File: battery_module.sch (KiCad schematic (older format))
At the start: 15 parts

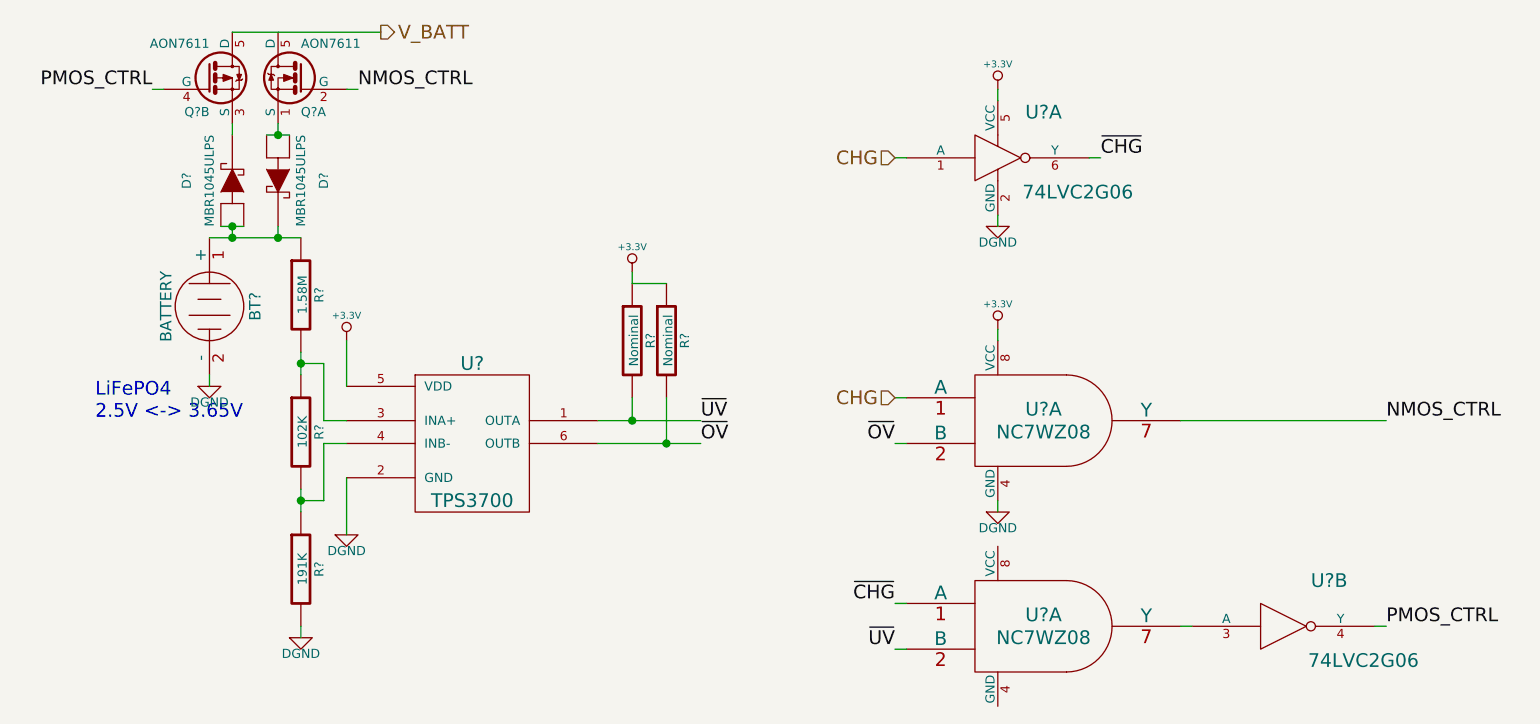
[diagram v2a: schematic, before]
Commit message: various fixes due to issues found in ERC
learned how to use invisible pins
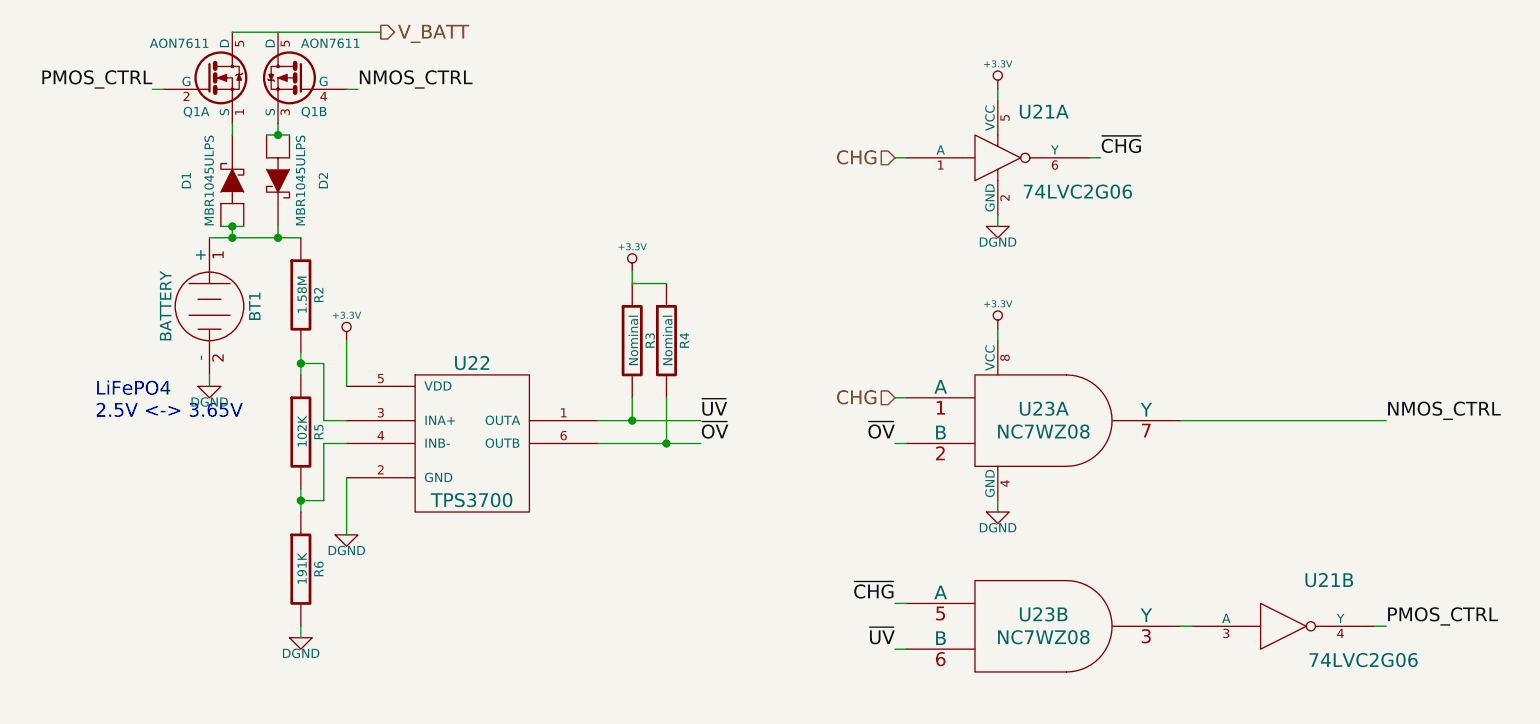
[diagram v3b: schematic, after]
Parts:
- gave numbers to parts that had none: 12
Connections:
- net NMOS_CTRL: now also Q2.4 (G); no longer Q2.2 (G)
- net PMOS_CTRL: now also Q2.2 (G); no longer Q2.4 (G)
- net ~CHG: now also U26.5 (A); no longer U26.1 (A)
- net ~UV: now also U26.6 (B); no longer U26.2 (B)
- net at U24.3 (A): now also U26.3 (Y); no longer U26.7 (Y)
- net at D4.1 (Anode), D4.2 (Anode): now also Q2.3 (S); no longer Q2.1 (S)
- net at D3.3 (Cathode): now also Q2.1 (S); no longer Q2.3 (S)

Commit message: gave parts unique id's
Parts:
- renumbered BT2 to BT1, D3 to D1, D4 to D2, Q2 to Q1, R7 to R2, R8 to R3, R9 to R4, R10 to R5, R11 to R6, U24 to U21, U25 to U22, U26 to U23
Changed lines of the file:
@@
 $Descr A4 11693 8268
 encoding utf-8
-Sheet 4 18
+Sheet 3 18
 Title ""
-Date "21 dec 2013"
+Date "12 jan 2014"
 Rev ""
 Comp ""
@@
 $EndDescr
 $Comp
-L BATTERY BT2
+L BATTERY BT1
 U 1 1 5281D336
 P 1300 1800
+AR Path="/5224C457/5281D330/5281D336" Ref="BT1"  Part="1"
 AR Path="/5224C457/5281E180/5281D336" Ref="BT2"  Part="1"
-AR Path="/5224C457/5281D330/5281D336" Ref="BT1"  Part="1"
 AR Path="/5224C457/5281E2A4/5281D336" Ref="BT3"  Part="1"
 F 0 "BT1" H 1300 2000 50  0000 C CNN
@@
 $EndComp
 $Comp
-L TPS3700 U25
+L TPS3700 U22
 U 1 1 5281D33C
 P 2450 2100
+AR Path="/5224C457/5281D330/5281D33C" Ref="U22"  Part="1"
 AR Path="/5224C457/5281E180/5281D33C" Ref="U25"  Part="1"
-AR Path="/5224C457/5281D330/5281D33C" Ref="U22"  Part="1"
 AR Path="/5224C457/5281E2A4/5281D33C" Ref="U28"  Part="1"
 F 0 "U22" H 2450 2150 60  0000 C CNN
@@
 $EndComp
 $Comp
-L R R7
+L R R2
 U 1 1 5281D342
 P 1700 1750
+AR Path="/5224C457/5281D330/5281D342" Ref="R2"  Part="1"
 AR Path="/5224C457/5281E180/5281D342" Ref="R7"  Part="1"
-AR Path="/5224C457/5281D330/5281D342" Ref="R2"  Part="1"
 AR Path="/5224C457/5281E2A4/5281D342" Ref="R12"  Part="1"
 F 0 "R2" V 1780 1750 40  0000 C CNN
@@
 $EndComp
 $Comp
-L R R10
+L R R5
 U 1 1 5281D348
 P 1700 2350
+AR Path="/5224C457/5281D330/5281D348" Ref="R5"  Part="1"
 AR Path="/5224C457/5281E180/5281D348" Ref="R10"  Part="1"
-AR Path="/5224C457/5281D330/5281D348" Ref="R5"  Part="1"
 AR Path="/5224C457/5281E2A4/5281D348" Ref="R15"  Part="1"
 F 0 "R5" V 1780 2350 40  0000 C CNN
@@
 $EndComp
 $Comp
-L R R11
+L R R6
 U 1 1 5281D34E
 P 1700 2950
+AR Path="/5224C457/5281D330/5281D34E" Ref="R6"  Part="1"
 AR Path="/5224C457/5281E180/5281D34E" Ref="R11"  Part="1"
-AR Path="/5224C457/5281D330/5281D34E" Ref="R6"  Part="1"
 AR Path="/5224C457/5281E2A4/5281D34E" Ref="R16"  Part="1"
 F 0 "R6" V 1780 2950 40  0000 C CNN
@@
 $EndComp
 $Comp
-L DGND #PWR017
+L DGND #PWR08
 U 1 1 5281D354
 P 1700 3250
+AR Path="/5224C457/5281D330/5281D354" Ref="#PWR08"  Part="1"
 AR Path="/5224C457/5281E180/5281D354" Ref="#PWR017"  Part="1"
-AR Path="/5224C457/5281D330/5281D354" Ref="#PWR08"  Part="1"
 AR Path="/5224C457/5281E2A4/5281D354" Ref="#PWR026"  Part="1"
 F 0 "#PWR08" H 1700 3250 40  0001 C CNN
@@
 $EndComp
 $Comp
-L DGND #PWR018
+L DGND #PWR09
 U 1 1 5281D35A
 P 1300 2150
+AR Path="/5224C457/5281D330/5281D35A" Ref="#PWR09"  Part="1"
 AR Path="/5224C457/5281E180/5281D35A" Ref="#PWR018"  Part="1"
-AR Path="/5224C457/5281D330/5281D35A" Ref="#PWR09"  Part="1"
 AR Path="/5224C457/5281E2A4/5281D35A" Ref="#PWR027"  Part="1"
 F 0 "#PWR09" H 1300 2150 40  0001 C CNN
@@
 $EndComp
 $Comp
-L DGND #PWR019
+L DGND #PWR010
 U 1 1 5281D360
 P 1900 2800
+AR Path="/5224C457/5281D330/5281D360" Ref="#PWR010"  Part="1"
 AR Path="/5224C457/5281E180/5281D360" Ref="#PWR019"  Part="1"
-AR Path="/5224C457/5281D330/5281D360" Ref="#PWR010"  Part="1"
 AR Path="/5224C457/5281E2A4/5281D360" Ref="#PWR028"  Part="1"
 F 0 "#PWR010" H 1900 2800 40  0001 C CNN
@@
 $EndComp
 $Comp
-L +3.3V #PWR020
+L +3.3V #PWR011
 U 1 1 5281D366
 P 1900 1950
+AR Path="/5224C457/5281D330/5281D366" Ref="#PWR011"  Part="1"
 AR Path="/5224C457/5281E180/5281D366" Ref="#PWR020"  Part="1"
-AR Path="/5224C457/5281D330/5281D366" Ref="#PWR011"  Part="1"
 AR Path="/5224C457/5281E2A4/5281D366" Ref="#PWR029"  Part="1"
 F 0 "#PWR011" H 1900 1910 30  0001 C CNN
@@
 $EndComp
 $Comp
-L R R8
+L R R3
 U 1 1 5281D36C
 P 3150 1950
+AR Path="/5224C457/5281D330/5281D36C" Ref="R3"  Part="1"
 AR Path="/5224C457/5281E180/5281D36C" Ref="R8"  Part="1"
-AR Path="/5224C457/5281D330/5281D36C" Ref="R3"  Part="1"
 AR Path="/5224C457/5281E2A4/5281D36C" Ref="R13"  Part="1"
 F 0 "R3" V 3230 1950 40  0000 C CNN
@@
 $EndComp
 $Comp
-L R R9
+L R R4
 U 1 1 5281D372
 P 3300 1950
+AR Path="/5224C457/5281D330/5281D372" Ref="R4"  Part="1"
 AR Path="/5224C457/5281E180/5281D372" Ref="R9"  Part="1"
-AR Path="/5224C457/5281D330/5281D372" Ref="R4"  Part="1"
 AR Path="/5224C457/5281E2A4/5281D372" Ref="R14"  Part="1"
 F 0 "R4" V 3380 1950 40  0000 C CNN
@@
 $EndComp
 $Comp
-L +3.3V #PWR021
+L +3.3V #PWR012
 U 1 1 5281D378
 P 3150 1650
+AR Path="/5224C457/5281D330/5281D378" Ref="#PWR012"  Part="1"
 AR Path="/5224C457/5281E180/5281D378" Ref="#PWR021"  Part="1"
-AR Path="/5224C457/5281D330/5281D378" Ref="#PWR012"  Part="1"
 AR Path="/5224C457/5281E2A4/5281D378" Ref="#PWR030"  Part="1"
 F 0 "#PWR012" H 3150 1610 30  0001 C CNN
@@
 CHG
 $Comp
-L 74LVC2G06 U24
+L 74LVC2G06 U21
 U 1 1 5281D380
 P 4750 1150
+AR Path="/5224C457/5281D330/5281D380" Ref="U21"  Part="1"
 AR Path="/5224C457/5281E180/5281D380" Ref="U24"  Part="1"
-AR Path="/5224C457/5281D330/5281D380" Ref="U21"  Part="1"
 AR Path="/5224C457/5281E2A4/5281D380" Ref="U27"  Part="1"
 F 0 "U21" H 4950 1350 60  0000 C CNN
@@
 $EndComp
 $Comp
-L 74LVC2G06 U24
+L 74LVC2G06 U21
 U 2 1 5281D386
 P 6000 3200
+AR Path="/5224C457/5281D330/5281D386" Ref="U21"  Part="2"
 AR Path="/5224C457/5281E180/5281D386" Ref="U24"  Part="2"
-AR Path="/5224C457/5281D330/5281D386" Ref="U21"  Part="2"
 AR Path="/5224C457/5281E2A4/5281D386" Ref="U27"  Part="2"
 F 0 "U21" H 6200 3400 60  0000 C CNN
@@
 $EndComp
 $Comp
-L DGND #PWR022
+L DGND #PWR013
 U 1 1 5281D38C
 P 4750 1450
+AR Path="/5224C457/5281D330/5281D38C" Ref="#PWR013"  Part="1"
 AR Path="/5224C457/5281E180/5281D38C" Ref="#PWR022"  Part="1"
-AR Path="/5224C457/5281D330/5281D38C" Ref="#PWR013"  Part="1"
 AR Path="/5224C457/5281E2A4/5281D38C" Ref="#PWR031"  Part="1"
 F 0 "#PWR013" H 4750 1450 40  0001 C CNN
@@
 $EndComp
 $Comp
-L +3.3V #PWR023
+L +3.3V #PWR014
 U 1 1 5281D392
 P 4750 850
+AR Path="/5224C457/5281D330/5281D392" Ref="#PWR014"  Part="1"
 AR Path="/5224C457/5281E180/5281D392" Ref="#PWR023"  Part="1"
-AR Path="/5224C457/5281D330/5281D392" Ref="#PWR014"  Part="1"
 AR Path="/5224C457/5281E2A4/5281D392" Ref="#PWR032"  Part="1"
 F 0 "#PWR014" H 4750 810 30  0001 C CNN
@@
 $EndComp
 $Comp
-L NC7WZ08 U26
+L NC7WZ08 U23
 U 1 1 5281D398
 P 4950 2300
+AR Path="/5224C457/5281D330/5281D398" Ref="U23"  Part="1"
 AR Path="/5224C457/5281E180/5281D398" Ref="U26"  Part="1"
-AR Path="/5224C457/5281D330/5281D398" Ref="U23"  Part="1"
 AR Path="/5224C457/5281E2A4/5281D398" Ref="U29"  Part="1"
 F 0 "U23" H 4950 2350 60  0000 C CNN
@@
 $EndComp
 $Comp
-L NC7WZ08 U26
+L NC7WZ08 U23
 U 2 1 5281D39E
 P 4950 3200
+AR Path="/5224C457/5281D330/5281D39E" Ref="U23"  Part="2"
 AR Path="/5224C457/5281E180/5281D39E" Ref="U26"  Part="2"
-AR Path="/5224C457/5281D330/5281D39E" Ref="U23"  Part="2"
 AR Path="/5224C457/5281E2A4/5281D39E" Ref="U29"  Part="2"
 F 0 "U23" H 4950 3250 60  0000 C CNN
@@
 NMOS_CTRL
 $Comp
-L DGND #PWR024
+L DGND #PWR015
 U 1 1 5281D3A6
 P 4750 2700
+AR Path="/5224C457/5281D330/5281D3A6" Ref="#PWR015"  Part="1"
 AR Path="/5224C457/5281E180/5281D3A6" Ref="#PWR024"  Part="1"
-AR Path="/5224C457/5281D330/5281D3A6" Ref="#PWR015"  Part="1"
 AR Path="/5224C457/5281E2A4/5281D3A6" Ref="#PWR033"  Part="1"
 F 0 "#PWR015" H 4750 2700 40  0001 C CNN
@@
 $EndComp
 $Comp
-L +3.3V #PWR025
+L +3.3V #PWR016
 U 1 1 5281D3AC
 P 4750 1900
+AR Path="/5224C457/5281D330/5281D3AC" Ref="#PWR016"  Part="1"
 AR Path="/5224C457/5281E180/5281D3AC" Ref="#PWR025"  Part="1"
-AR Path="/5224C457/5281D330/5281D3AC" Ref="#PWR016"  Part="1"
 AR Path="/5224C457/5281E2A4/5281D3AC" Ref="#PWR034"  Part="1"
 F 0 "#PWR016" H 4750 1860 30  0001 C CNN
@@
 ~CHG
 $Comp
-L AON7611 Q2
+L AON7611 Q1
 U 2 1 5281D3B9
 P 1700 800
+AR Path="/5224C457/5281D330/5281D3B9" Ref="Q1"  Part="2"
 AR Path="/5224C457/5281E180/5281D3B9" Ref="Q2"  Part="2"
-AR Path="/5224C457/5281D330/5281D3B9" Ref="Q1"  Part="2"
 AR Path="/5224C457/5281E2A4/5281D3B9" Ref="Q3"  Part="2"
 F 0 "Q1" H 1700 651 40  0000 R CNN
@@
 $EndComp
 $Comp
-L AON7611 Q2
+L AON7611 Q1
 U 1 1 5281D3BF
 P 1300 800
+AR Path="/5224C457/5281D330/5281D3BF" Ref="Q1"  Part="1"
 AR Path="/5224C457/5281E180/5281D3BF" Ref="Q2"  Part="1"
-AR Path="/5224C457/5281D330/5281D3BF" Ref="Q1"  Part="1"
 AR Path="/5224C457/5281E2A4/5281D3BF" Ref="Q3"  Part="1"
 F 0 "Q1" H 1300 651 40  0000 R CNN
@@
 PMOS_CTRL
 $Comp
-L MBR1045ULPS D3
+L MBR1045ULPS D1
 U 1 1 5281D3C7
 P 1400 1250
+AR Path="/5224C457/5281D330/5281D3C7" Ref="D1"  Part="1"
 AR Path="/5224C457/5281E180/5281D3C7" Ref="D3"  Part="1"
-AR Path="/5224C457/5281D330/5281D3C7" Ref="D1"  Part="1"
 AR Path="/5224C457/5281E2A4/5281D3C7" Ref="D5"  Part="1"
 F 0 "D1" H 1400 1450 40  0000 C CNN
@@
 $EndComp
 $Comp
-L MBR1045ULPS D4
+L MBR1045ULPS D2
 U 1 1 5281D3CD
 P 1600 1250
+AR Path="/5224C457/5281D330/5281D3CD" Ref="D2"  Part="1"
 AR Path="/5224C457/5281E180/5281D3CD" Ref="D4"  Part="1"
-AR Path="/5224C457/5281D330/5281D3CD" Ref="D2"  Part="1"
 AR Path="/5224C457/5281E2A4/5281D3CD" Ref="D6"  Part="1"
 F 0 "D2" H 1600 1450 40  0000 C CNN
